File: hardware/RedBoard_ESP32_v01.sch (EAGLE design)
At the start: 112 parts, among them J1 5.5x2.1mm Barrel, J13 QWIIC_RIGHT_ANGLE, J15 MICRO-SD-PUSH-PUSH-EXT-PIN, J2 USB C, J3 USB_SOLDER_PADS, J5 M10NO_SILK, Q1 MBT3904DW1T1, Q11 20V/4.2A/52mΩ/1.4W, Q13 20V/4.2A/52mΩ/1.4W, Q3 20V/4.2A/52mΩ/1.4W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

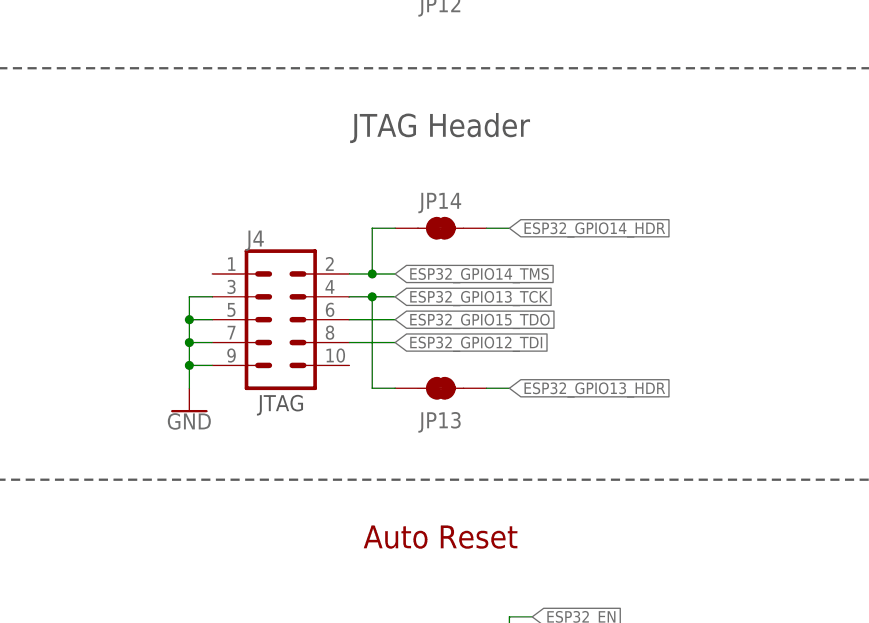
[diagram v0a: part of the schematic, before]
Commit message: Added Test Point per Eric Orosel request.
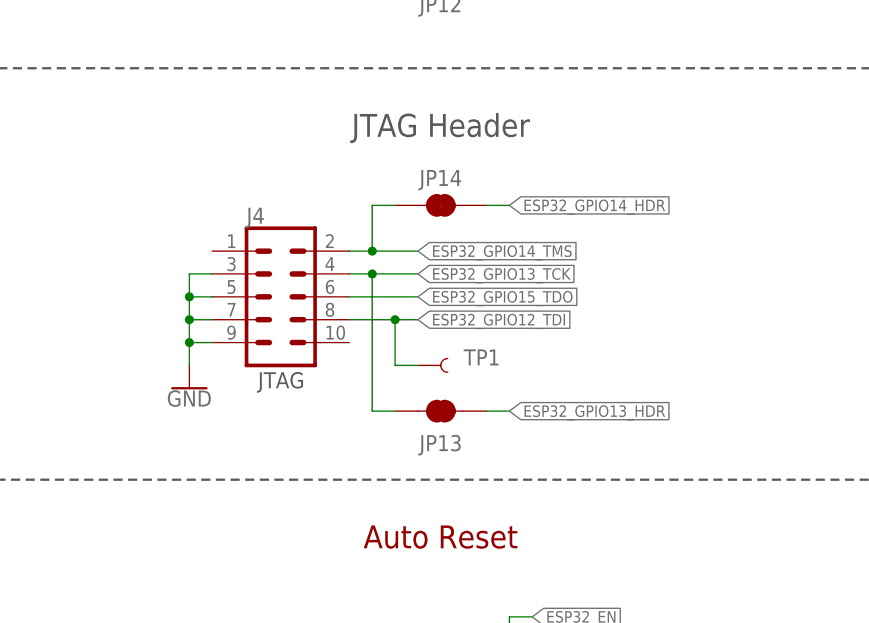
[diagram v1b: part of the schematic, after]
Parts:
- added TP1: TEST-POINT3, SparkFun-Connectors:TEST-POINT3
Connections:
- net ESP32_GPIO12_TDI: now also TP1.1
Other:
- moved on the sheet: J4, JP13, JP14
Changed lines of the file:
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@@
 <part name="GND53" library="SparkFun-PowerSymbols" deviceset="GND" device=""/>
 <part name="LOGO6" library="SparkFun-Aesthetics" deviceset="SFE_LOGO_NAME_FLAME" device=".2_INCH" value="SFE_LOGO_NAME_FLAME.2_INCH"/>
+<part name="TP1" library="SparkFun-Connectors" deviceset="TEST-POINT" device="3"/>
 </parts>
 <sheets>
@@
 <text x="254" y="254" size="1.778" layer="97" font="vector">This is the penny-in-the-fuse jumper.
 Close only if you know what you're doing.</text>
-<text x="30.48" y="101.6" size="1.778" layer="97">JTAG</text>
+<text x="30.48" y="104.14" size="1.778" layer="97">JTAG</text>
 <text x="184.15" y="264.922" size="1.27" layer="96">J6</text>
 <text x="135.636" y="264.922" size="1.27" layer="96">J5</text>
@@
 <attribute name="VALUE" x="139.954" y="210.82" size="1.778" layer="96" font="vector" rot="R270"/>
 </instance>
-<instance part="J4" gate="G$1" x="33.02" y="111.76" smashed="yes">
-<attribute name="VALUE" x="29.21" y="101.854" size="1.778" layer="96" font="vector"/>
-<attribute name="NAME" x="29.21" y="119.888" size="1.778" layer="95" font="vector"/>
+<instance part="J4" gate="G$1" x="33.02" y="114.3" smashed="yes">
+<attribute name="VALUE" x="29.21" y="104.394" size="1.778" layer="96" font="vector"/>
+<attribute name="NAME" x="29.21" y="122.428" size="1.778" layer="95" font="vector"/>
 </instance>
 <instance part="R7" gate="G$1" x="45.72" y="53.34" smashed="yes">
@@
 <attribute name="VALUE" x="231.14" y="4.826" size="1.778" layer="96" align="top-center"/>
 </instance>
-<instance part="GND1" gate="1" x="22.86" y="101.6" smashed="yes">
-<attribute name="VALUE" x="22.86" y="101.346" size="1.778" layer="96" align="top-center"/>
+<instance part="GND1" gate="1" x="22.86" y="104.14" smashed="yes">
+<attribute name="VALUE" x="22.86" y="103.886" size="1.778" layer="96" align="top-center"/>
 </instance>
 <instance part="JP11" gate="G$1" x="406.4" y="63.5" smashed="yes" rot="R270">
@@
 <attribute name="VALUE" x="254" y="213.106" size="1.778" layer="96" align="top-center"/>
 </instance>
-<instance part="JP13" gate="G$1" x="50.8" y="104.14" smashed="yes">
-<attribute name="NAME" x="50.8" y="100.584" size="1.778" layer="95" font="vector" align="center"/>
-<attribute name="VALUE" x="50.8" y="101.092" size="1.778" layer="96" font="vector" align="center" display="off"/>
-</instance>
-<instance part="JP14" gate="G$1" x="50.8" y="121.92" smashed="yes">
-<attribute name="NAME" x="50.8" y="124.968" size="1.778" layer="95" font="vector" align="center"/>
-<attribute name="VALUE" x="50.8" y="118.872" size="1.778" layer="96" font="vector" align="center" display="off"/>
+<instance part="JP13" gate="G$1" x="50.8" y="101.6" smashed="yes">
+<attribute name="NAME" x="50.8" y="98.044" size="1.778" layer="95" font="vector" align="center"/>
+<attribute name="VALUE" x="50.8" y="98.552" size="1.778" layer="96" font="vector" align="center" display="off"/>
+</instance>
+<instance part="JP14" gate="G$1" x="50.8" y="124.46" smashed="yes">
+<attribute name="NAME" x="50.8" y="127.508" size="1.778" layer="95" font="vector" align="center"/>
+<attribute name="VALUE" x="50.8" y="121.412" size="1.778" layer="96" font="vector" align="center" display="off"/>
 </instance>
 <instance part="C10" gate="G$1" x="170.18" y="121.92" smashed="yes">
@@
 </instance>
 <instance part="LOGO6" gate="G$1" x="247.65" y="4.826" smashed="yes"/>
+<instance part="TP1" gate="G$1" x="48.26" y="106.68" smashed="yes">
+<attribute name="NAME" x="53.34" y="106.68" size="1.778" layer="95" font="vector"/>
+<attribute name="VALUE" x="45.72" y="104.14" size="1.778" layer="96" font="vector" display="off"/>
+</instance>
 </instances>
 <busses>
@@
 <segment>
 <pinref part="J4" gate="G$1" pin="3"/>
-<wire x1="25.4" y1="114.3" x2="22.86" y2="114.3" width="0.1524" layer="91"/>
+<wire x1="25.4" y1="116.84" x2="22.86" y2="116.84" width="0.1524" layer="91"/>
+<wire x1="22.86" y1="116.84" x2="22.86" y2="114.3" width="0.1524" layer="91"/>
+<pinref part="J4" gate="G$1" pin="9"/>
 <wire x1="22.86" y1="114.3" x2="22.86" y2="111.76" width="0.1524" layer="91"/>
-<pinref part="J4" gate="G$1" pin="9"/>
 <wire x1="22.86" y1="111.76" x2="22.86" y2="109.22" width="0.1524" layer="91"/>
 <wire x1="22.86" y1="109.22" x2="22.86" y2="106.68" width="0.1524" layer="91"/>
-<wire x1="22.86" y1="106.68" x2="22.86" y2="104.14" width="0.1524" layer="91"/>
-<wire x1="25.4" y1="106.68" x2="22.86" y2="106.68" width="0.1524" layer="91"/>
-<junction x="22.86" y="106.68"/>
-<pinref part="J4" gate="G$1" pin="7"/>
 <wire x1="25.4" y1="109.22" x2="22.86" y2="109.22" width="0.1524" layer="91"/>
 <junction x="22.86" y="109.22"/>
-<pinref part="J4" gate="G$1" pin="5"/>
+<pinref part="J4" gate="G$1" pin="7"/>
 <wire x1="25.4" y1="111.76" x2="22.86" y2="111.76" width="0.1524" layer="91"/>
 <junction x="22.86" y="111.76"/>
+<pinref part="J4" gate="G$1" pin="5"/>
+<wire x1="25.4" y1="114.3" x2="22.86" y2="114.3" width="0.1524" layer="91"/>
+<junction x="22.86" y="114.3"/>
 <pinref part="GND1" gate="1" pin="GND"/>
 </segment>
@@
 <segment>
 <pinref part="J4" gate="G$1" pin="8"/>
-<wire x1="40.64" y1="109.22" x2="45.72" y2="109.22" width="0.1524" layer="91"/>
-<label x="45.72" y="109.22" size="1.27" layer="95" xref="yes"/>
+<wire x1="40.64" y1="111.76" x2="45.72" y2="111.76" width="0.1524" layer="91"/>
+<label x="48.26" y="111.76" size="1.27" layer="95" xref="yes"/>
+<wire x1="45.72" y1="111.76" x2="48.26" y2="111.76" width="0.1524" layer="91"/>
+<wire x1="45.72" y1="111.76" x2="45.72" y2="106.68" width="0.1524" layer="91"/>
+<junction x="45.72" y="111.76"/>
+<wire x1="45.72" y1="106.68" x2="48.26" y2="106.68" width="0.1524" layer="91"/>
+<pinref part="TP1" gate="G$1" pin="1"/>
 </segment>
 <segment>
@@
 <segment>
 <pinref part="J4" gate="G$1" pin="4"/>
-<wire x1="40.64" y1="114.3" x2="43.18" y2="114.3" width="0.1524" layer="91"/>
-<label x="45.72" y="114.3" size="1.27" layer="95" xref="yes"/>
-<wire x1="43.18" y1="114.3" x2="45.72" y2="114.3" width="0.1524" layer="91"/>
-<wire x1="43.18" y1="114.3" x2="43.18" y2="104.14" width="0.1524" layer="91"/>
-<junction x="43.18" y="114.3"/>
+<wire x1="40.64" y1="116.84" x2="43.18" y2="116.84" width="0.1524" layer="91"/>
+<label x="48.26" y="116.84" size="1.27" layer="95" xref="yes"/>
+<wire x1="43.18" y1="116.84" x2="48.26" y2="116.84" width="0.1524" layer="91"/>
+<wire x1="43.18" y1="116.84" x2="43.18" y2="101.6" width="0.1524" layer="91"/>
+<junction x="43.18" y="116.84"/>
 <pinref part="JP13" gate="G$1" pin="1"/>
-<wire x1="43.18" y1="104.14" x2="45.72" y2="104.14" width="0.1524" layer="91"/>
+<wire x1="43.18" y1="101.6" x2="45.72" y2="101.6" width="0.1524" layer="91"/>
 </segment>
 <segment>
@@
 <segment>
 <pinref part="J4" gate="G$1" pin="2"/>
-<wire x1="40.64" y1="116.84" x2="43.18" y2="116.84" width="0.1524" layer="91"/>
-<label x="45.72" y="116.84" size="1.27" layer="95" xref="yes"/>
+<wire x1="40.64" y1="119.38" x2="43.18" y2="119.38" width="0.1524" layer="91"/>
+<label x="48.26" y="119.38" size="1.27" layer="95" xref="yes"/>
 <pinref part="JP14" gate="G$1" pin="1"/>
-<wire x1="43.18" y1="116.84" x2="45.72" y2="116.84" width="0.1524" layer="91"/>
-<wire x1="45.72" y1="121.92" x2="43.18" y2="121.92" width="0.1524" layer="91"/>
-<wire x1="43.18" y1="121.92" x2="43.18" y2="116.84" width="0.1524" layer="91"/>
-<junction x="43.18" y="116.84"/>
+<wire x1="43.18" y1="119.38" x2="48.26" y2="119.38" width="0.1524" layer="91"/>
+<wire x1="45.72" y1="124.46" x2="43.18" y2="124.46" width="0.1524" layer="91"/>
+<wire x1="43.18" y1="124.46" x2="43.18" y2="119.38" width="0.1524" layer="91"/>
+<junction x="43.18" y="119.38"/>
 </segment>
 <segment>
@@
 <segment>
 <pinref part="J4" gate="G$1" pin="6"/>
-<wire x1="40.64" y1="111.76" x2="45.72" y2="111.76" width="0.1524" layer="91"/>
-<label x="45.72" y="111.76" size="1.27" layer="95" xref="yes"/>
+<wire x1="40.64" y1="114.3" x2="48.26" y2="114.3" width="0.1524" layer="91"/>
+<label x="48.26" y="114.3" size="1.27" layer="95" xref="yes"/>
 </segment>
 </net>
@@
 <segment>
 <pinref part="JP14" gate="G$1" pin="2"/>
-<wire x1="55.88" y1="121.92" x2="58.42" y2="121.92" width="0.1524" layer="91"/>
-<label x="58.42" y="121.92" size="1.27" layer="95" xref="yes"/>
+<wire x1="55.88" y1="124.46" x2="58.42" y2="124.46" width="0.1524" layer="91"/>
+<label x="58.42" y="124.46" size="1.27" layer="95" xref="yes"/>
 </segment>
 <segment>
@@
 <segment>
 <pinref part="JP13" gate="G$1" pin="2"/>
-<wire x1="55.88" y1="104.14" x2="58.42" y2="104.14" width="0.1524" layer="91"/>
-<label x="58.42" y="104.14" size="1.27" layer="95" xref="yes"/>
-</segment>
-<segment>
+<wire x1="55.88" y1="101.6" x2="58.42" y2="101.6" width="0.1524" layer="91"/>
+<label x="58.42" y="101.6" size="1.27" layer="95" xref="yes"/>
+</segment>
+<segment>
